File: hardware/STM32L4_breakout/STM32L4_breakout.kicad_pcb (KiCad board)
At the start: 2 copper layers, 84.8 x 91.2 mm, 67 parts, among them J1 12V IN, J10 GPIO, J11 SPI1, J12 USART1, J13 USART3, J14 UART4, J15 3.3V, J16 5V, J17 12V, J2 SWD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

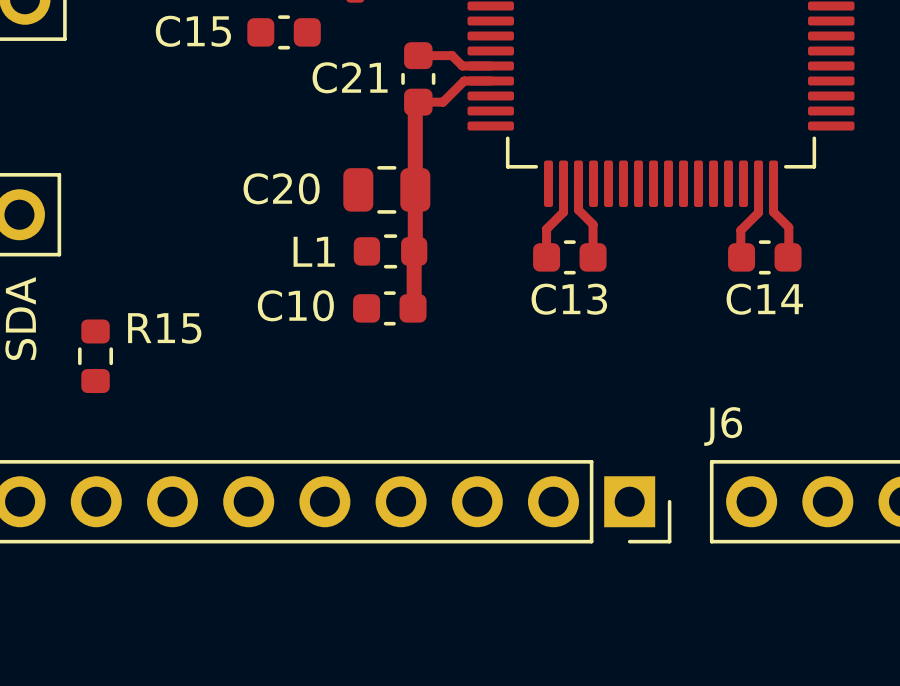
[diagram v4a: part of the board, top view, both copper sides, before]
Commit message: routed SPI lines
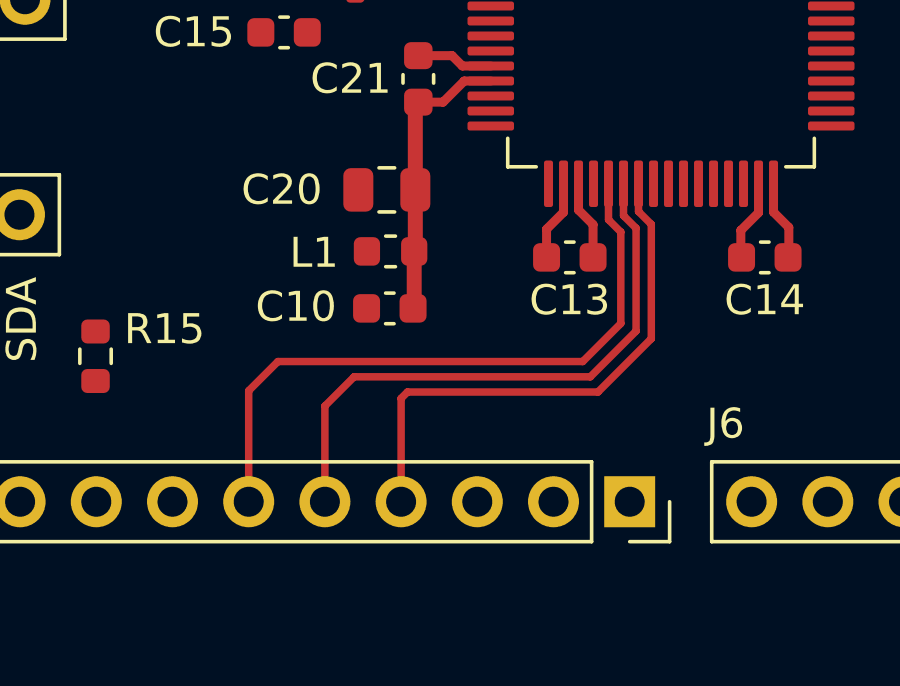
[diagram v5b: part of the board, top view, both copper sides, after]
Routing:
- net SPI1_SCK: track 0.00 -> 21.9 mm
- net SPI1_MISO: track 0.00 -> 19.7 mm
- net SPI1_MOSI: track 0.00 -> 18.0 mm
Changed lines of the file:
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@@
   (segment (start 142.808 65.264) (end 142.788 65.284) (width 0.3) (layer "F.Cu") (net 9))
   (segment (start 142.088 65.764) (end 140.788 65.764) (width 0.3) (layer "F.Cu") (net 9))
+  (segment (start 152.228 73.485208) (end 152.654 73.911208) (width 0.25) (layer "F.Cu") (net 25))
+  (segment (start 150.876 79.502) (end 144.526 79.502) (width 0.25) (layer "F.Cu") (net 25))
+  (segment (start 144.314 79.714) (end 144.314 83.159) (width 0.25) (layer "F.Cu") (net 25))
+  (segment (start 144.526 79.502) (end 144.314 79.714) (width 0.25) (layer "F.Cu") (net 25))
+  (segment (start 152.654 73.911208) (end 152.654 77.724) (width 0.25) (layer "F.Cu") (net 25))
+  (segment (start 152.228 72.559) (end 152.228 73.485208) (width 0.25) (layer "F.Cu") (net 25))
+  (segment (start 152.654 77.724) (end 150.876 79.502) (width 0.25) (layer "F.Cu") (net 25))
+  (segment (start 151.728 73.621604) (end 152.146 74.039604) (width 0.25) (layer "F.Cu") (net 26))
+  (segment (start 142.748 78.994) (end 141.774 79.968) (width 0.25) (layer "F.Cu") (net 26))
+  (segment (start 141.774 79.968) (end 141.774 83.159) (width 0.25) (layer "F.Cu") (net 26))
+  (segment (start 152.146 77.47) (end 150.622 78.994) (width 0.25) (layer "F.Cu") (net 26))
+  (segment (start 152.146 74.039604) (end 152.146 77.47) (width 0.25) (layer "F.Cu") (net 26))
+  (segment (start 150.622 78.994) (end 142.748 78.994) (width 0.25) (layer "F.Cu") (net 26))
+  (segment (start 151.728 72.559) (end 151.728 73.621604) (width 0.25) (layer "F.Cu") (net 26))
+  (segment (start 139.234 83.159) (end 139.234 79.46) (width 0.25) (layer "F.Cu") (net 27))
+  (segment (start 150.368 78.486) (end 151.638 77.216) (width 0.25) (layer "F.Cu") (net 27))
+  (segment (start 139.234 79.46) (end 140.208 78.486) (width 0.25) (layer "F.Cu") (net 27))
+  (segment (start 151.228 73.758) (end 151.228 72.559) (width 0.25) (layer "F.Cu") (net 27))
+  (segment (start 140.208 78.486) (end 150.368 78.486) (width 0.25) (layer "F.Cu") (net 27))
+  (segment (start 151.638 74.168) (end 151.228 73.758) (width 0.25) (layer "F.Cu") (net 27))
+  (segment (start 151.638 77.216) (end 151.638 74.168) (width 0.25) (layer "F.Cu") (net 27))
   (segment (start 146.358 64.134) (end 145.988 63.764) (width 0.3) (layer "F.Cu") (net 56))
   (segment (start 147.303 64.134) (end 146.358 64.134) (width 0.3) (layer "F.Cu") (net 56))

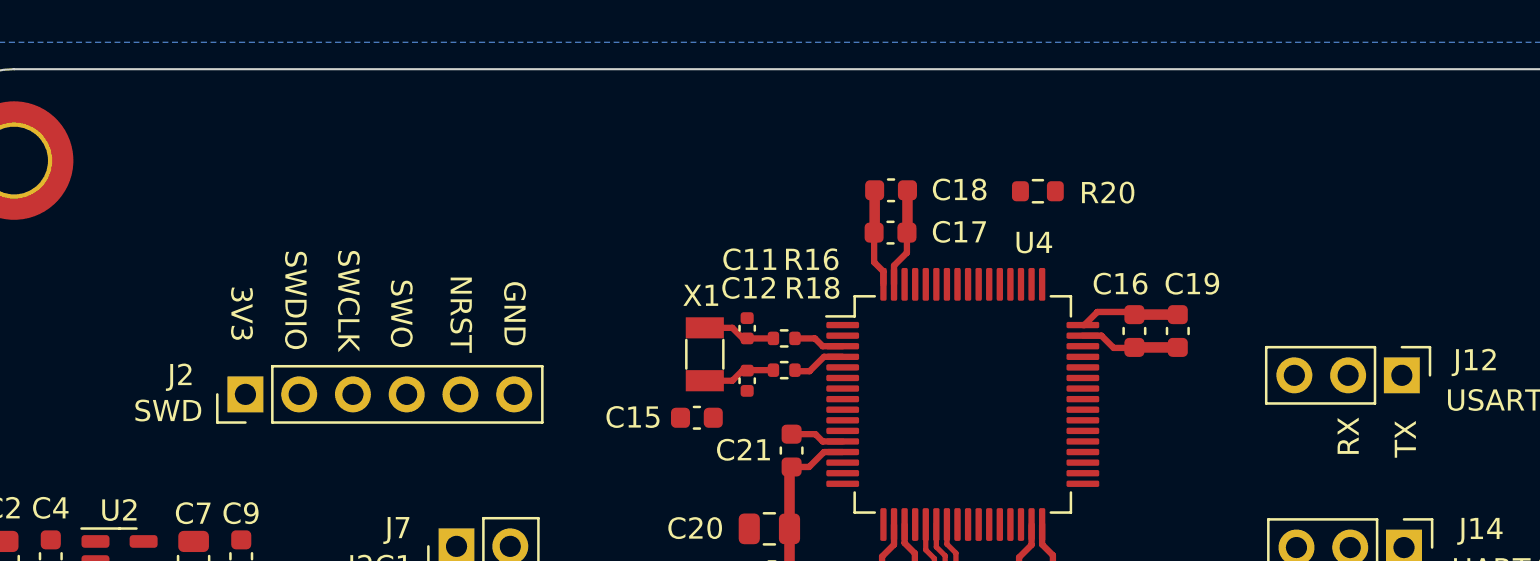
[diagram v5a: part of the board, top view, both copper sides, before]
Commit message: routed SWD on breakout board
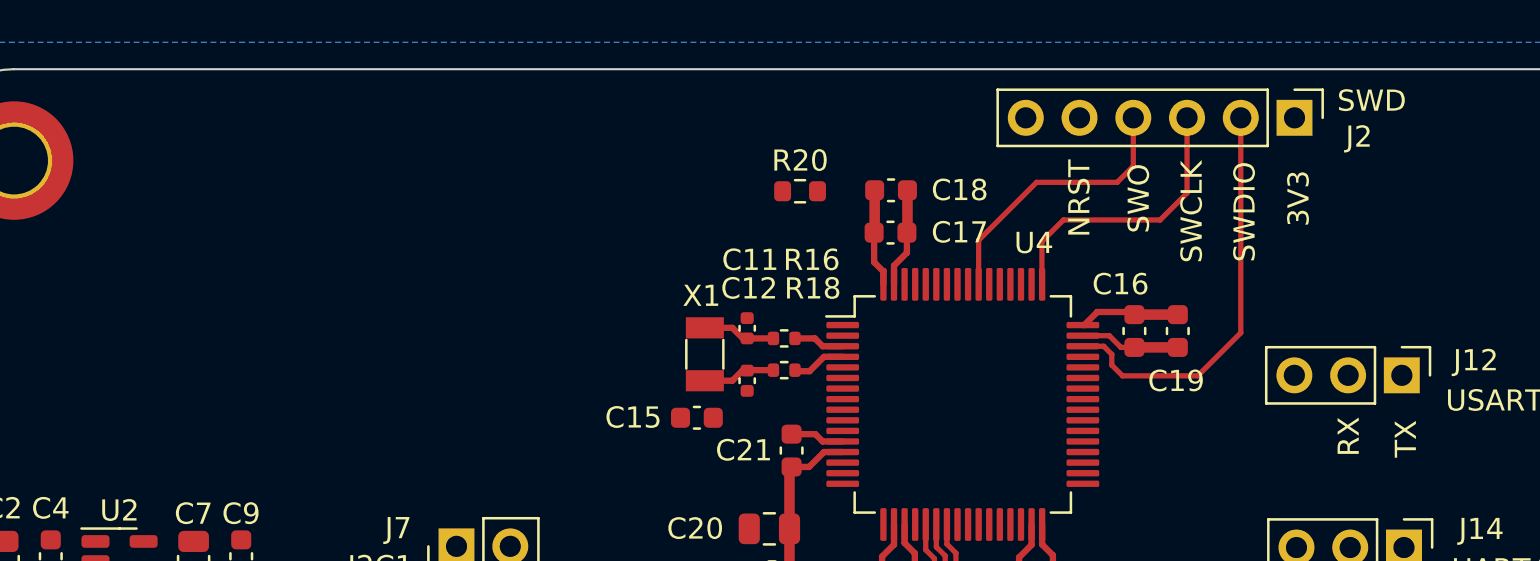
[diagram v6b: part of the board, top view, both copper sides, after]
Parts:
- moved J2 51.3 mm to (168.7, 53.3), turned to -90 degrees
- moved R20 11.2 mm to (145.3, 56.8), turned to 0 degrees
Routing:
- net SWDIO: track 0.00 -> 19.3 mm
- net SWCLK: track 0.00 -> 13.4 mm
- net SWO: track 0.00 -> 13.1 mm
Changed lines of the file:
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@@
   )
   (footprint "Resistor_SMD:R_0603_1608Metric" (layer "F.Cu")
-    (at 156.528 56.809 180)
+    (at 145.288 56.809)
     (descr "Resistor SMD 0603 (1608 Metric), square (rectangular) end terminal, IPC_7351 nominal, (Body size source: IPC-SM-782 page 72, https://www.pcb-3d.com/wordpress/wp-content/uploads/ipc-sm-782a_amendment_1_and_2.pdf), generated with kicad-footprint-generator")
     (tags "resistor")
@@
     (property "Sheetname" "")
     (attr smd)
-    (fp_text reference "R20" (at -3.3 -0.1) (layer "F.SilkS")
+    (fp_text reference "R20" (at 0 -1.437) (layer "F.SilkS")
       (effects (font (size 1 1) (thickness 0.15)))
     )
@@
     (fp_line (start 0.8 0.4125) (end -0.8 0.4125) (layer "F.Fab") (width 0.1))
     (fp_line (start -0.8 0.4125) (end -0.8 -0.4125) (layer "F.Fab") (width 0.1))
-    (pad "1" smd roundrect (at -0.825 0 180) (size 0.8 0.95) (layers "F.Cu" "F.Paste" "F.Mask") (roundrect_rratio 0.25)
+    (pad "1" smd roundrect (at -0.825 0) (size 0.8 0.95) (layers "F.Cu" "F.Paste" "F.Mask") (roundrect_rratio 0.25)
       (net 58 "Net-(R20-Pad1)") (pintype "passive"))
-    (pad "2" smd roundrect (at 0.825 0 180) (size 0.8 0.95) (layers "F.Cu" "F.Paste" "F.Mask") (roundrect_rratio 0.25)
+    (pad "2" smd roundrect (at 0.825 0) (size 0.8 0.95) (layers "F.Cu" "F.Paste" "F.Mask") (roundrect_rratio 0.25)
       (net 59 "/BOOT0") (pintype "passive"))
     (model "${KICAD6_3DMODEL_DIR}/Resistor_SMD.3dshapes/R_0603_1608Metric.wrl"
@@
   )
   (footprint "Connector_PinHeader_2.54mm:PinHeader_1x06_P2.54mm_Vertical" (layer "F.Cu")
-    (at 119.078 66.409 90)
+    (at 168.656 53.34 -90)
     (descr "Through hole straight pin header, 1x06, 2.54mm pitch, single row")
     (tags "Through hole pin header THT 1x06 2.54mm single row")
@@
     (property "Sheetname" "")
     (attr through_hole)
-    (fp_text reference "J2" (at 0.9 -3.05 180) (layer "F.SilkS")
-      (effects (font (size 1 1) (thickness 0.15)))
-    )
-    (fp_text value "SWD" (at -0.8 -3.65 180) (layer "F.SilkS")
-      (effects (font (size 1 1) (thickness 0.15)))
-    )
-    (fp_text user "SWO" (at 3.81 7.35 -90 unlocked) (layer "F.SilkS")
-      (effects (font (size 1 1) (thickness 0.15)))
-    )
-    (fp_text user "NRST" (at 3.81 10.16 -90 unlocked) (layer "F.SilkS")
-      (effects (font (size 1 1) (thickness 0.15)))
-    )
-    (fp_text user "SWDIO" (at 4.445 2.35 -90 unlocked) (layer "F.SilkS")
-      (effects (font (size 1 1) (thickness 0.15)))
-    )
-    (fp_text user "SWCLK" (at 4.445 4.85 -90 unlocked) (layer "F.SilkS")
-      (effects (font (size 1 1) (thickness 0.15)))
-    )
-    (fp_text user "3V3" (at 3.81 -0.2 -90 unlocked) (layer "F.SilkS")
-      (effects (font (size 1 1) (thickness 0.15)))
-    )
-    (fp_text user "GND" (at 3.81 12.7 -90 unlocked) (layer "F.SilkS")
+    (fp_text reference "J2" (at 0.9 -3.05) (layer "F.SilkS")
+      (effects (font (size 1 1) (thickness 0.15)))
+    )
+    (fp_text value "SWD" (at -0.8 -3.65) (layer "F.SilkS")
+      (effects (font (size 1 1) (thickness 0.15)))
+    )
+    (fp_text user "SWO" (at 3.81 7.35 -270 unlocked) (layer "F.SilkS")
+      (effects (font (size 1 1) (thickness 0.15)))
+    )
+    (fp_text user "NRST" (at 3.81 10.16 -270 unlocked) (layer "F.SilkS")
+      (effects (font (size 1 1) (thickness 0.15)))
+    )
+    (fp_text user "SWDIO" (at 4.445 2.35 -270 unlocked) (layer "F.SilkS")
+      (effects (font (size 1 1) (thickness 0.15)))
+    )
+    (fp_text user "SWCLK" (at 4.445 4.85 -270 unlocked) (layer "F.SilkS")
+      (effects (font (size 1 1) (thickness 0.15)))
+    )
+    (fp_text user "3V3" (at 3.81 -0.2 -270 unlocked) (layer "F.SilkS")
       (effects (font (size 1 1) (thickness 0.15)))
     )
@@
     (fp_line (start 1.27 13.97) (end -1.27 13.97) (layer "F.Fab") (width 0.1))
     (fp_line (start 1.27 -1.27) (end 1.27 13.97) (layer "F.Fab") (width 0.1))
-    (pad "1" thru_hole rect (at 0 0 90) (size 1.7 1.7) (drill 1) (layers *.Cu *.Mask)
+    (pad "1" thru_hole rect (at 0 0 270) (size 1.7 1.7) (drill 1) (layers *.Cu *.Mask)
       (net 5 "VMEM") (pinfunction "Pin_1") (pintype "passive"))
-    (pad "2" thru_hole oval (at 0 2.54 90) (size 1.7 1.7) (drill 1) (layers *.Cu *.Mask)
+    (pad "2" thru_hole oval (at 0 2.54 270) (size 1.7 1.7) (drill 1) (layers *.Cu *.Mask)
       (net 11 "SWDIO") (pinfunction "Pin_2") (pintype "passive"))
-    (pad "3" thru_hole oval (at 0 5.08 90) (size 1.7 1.7) (drill 1) (layers *.Cu *.Mask)
+    (pad "3" thru_hole oval (at 0 5.08 270) (size 1.7 1.7) (drill 1) (layers *.Cu *.Mask)
       (net 12 "SWCLK") (pinfunction "Pin_3") (pintype "passive"))
-    (pad "4" thru_hole oval (at 0 7.62 90) (size 1.7 1.7) (drill 1) (layers *.Cu *.Mask)
+    (pad "4" thru_hole oval (at 0 7.62 270) (size 1.7 1.7) (drill 1) (layers *.Cu *.Mask)
       (net 13 "SWO") (pinfunction "Pin_4") (pintype "passive"))
-    (pad "5" thru_hole oval (at 0 10.16 90) (size 1.7 1.7) (drill 1) (layers *.Cu *.Mask)
+    (pad "5" thru_hole oval (at 0 10.16 270) (size 1.7 1.7) (drill 1) (layers *.Cu *.Mask)
       (net 10 "STM_NRST") (pinfunction "Pin_5") (pintype "passive"))
-    (pad "6" thru_hole oval (at 0 12.7 90) (size 1.7 1.7) (drill 1) (layers *.Cu *.Mask)
+    (pad "6" thru_hole oval (at 0 12.7 270) (size 1.7 1.7) (drill 1) (layers *.Cu *.Mask)
       (net 2 "GND") (pinfunction "Pin_6") (pintype "passive"))
     (model "${KICAD6_3DMODEL_DIR}/Connector_PinHeader_2.54mm.3dshapes/PinHeader_1x06_P2.54mm_Vertical.wrl"
@@
     (property "Sheetname" "")
     (attr smd)
-    (fp_text reference "C19" (at -2.2 -0.7) (layer "F.SilkS")
+    (fp_text reference "C19" (at 2.372 0.07) (layer "F.SilkS")
       (effects (font (size 1 1) (thickness 0.15)))
     )
@@
   (segment (start 155.638 74.114) (end 155.638 74.989) (width 0.3) (layer "F.Cu") (net 2))
   (segment (start 149.238 74.939) (end 149.163 75.014) (width 0.3) (layer "F.Cu") (net 2))
+  (segment (start 158.653 63.634) (end 159.9 63.634) (width 0.25) (layer "F.Cu") (net 2))
+  (segment (start 159.9 63.634) (end 160.455 64.189) (width 0.25) (layer "F.Cu") (net 2))
   (segment (start 163.138 64.189) (end 161.088 64.189) (width 0.5) (layer "F.Cu") (net 2))
-  (segment (start 159.529041 63.634) (end 160.109041 64.214) (width 0.3) (layer "F.Cu") (net 2))
   (segment (start 150.338 59.714) (end 150.338 58.764) (width 0.3) (layer "F.Cu") (net 2))
   (segment (start 149.728 61.209) (end 149.728 60.324) (width 0.3) (layer "F.Cu") (net 2))
@@
   (segment (start 156.228 73.524) (end 155.638 74.114) (width 0.3) (layer "F.Cu") (net 2))
   (segment (start 150.363 56.764) (end 150.363 58.739) (width 0.5) (layer "F.Cu") (net 2))
-  (segment (start 160.109041 64.214) (end 161.063 64.214) (width 0.3) (layer "F.Cu") (net 2))
   (segment (start 161.063 64.214) (end 161.088 64.189) (width 0.3) (layer "F.Cu") (net 2))
-  (segment (start 158.653 63.634) (end 159.529041 63.634) (width 0.3) (layer "F.Cu") (net 2))
+  (segment (start 160.455 64.189) (end 161.088 64.189) (width 0.25) (layer "F.Cu") (net 2))
   (segment (start 146.013 68.289) (end 144.888 68.289) (width 0.3) (layer "F.Cu") (net 2))
   (segment (start 146.358 68.634) (end 146.013 68.289) (width 0.3) (layer "F.Cu") (net 2))
@@
   (segment (start 142.808 65.264) (end 142.788 65.284) (width 0.3) (layer "F.Cu") (net 9))
   (segment (start 142.088 65.764) (end 140.788 65.764) (width 0.3) (layer "F.Cu") (net 9))
+  (segment (start 164.084 65.532) (end 166.116 63.5) (width 0.25) (layer "F.Cu") (net 11))
+  (segment (start 158.653 64.134) (end 159.638 64.134) (width 0.25) (layer "F.Cu") (net 11))
+  (segment (start 160.02 64.516) (end 160.02 65.024) (width 0.25) (layer "F.Cu") (net 11))
+  (segment (start 160.528 65.532) (end 164.084 65.532) (width 0.25) (layer "F.Cu") (net 11))
+  (segment (start 160.02 65.024) (end 160.528 65.532) (width 0.25) (layer "F.Cu") (net 11))
+  (segment (start 166.116 63.5) (end 166.116 53.34) (width 0.25) (layer "F.Cu") (net 11))
+  (segment (start 159.638 64.134) (end 160.02 64.516) (width 0.25) (layer "F.Cu") (net 11))
+  (segment (start 156.728 61.209) (end 156.718 61.199) (width 0.25) (layer "F.Cu") (net 12))
+  (segment (start 157.734 58.166) (end 162.306 58.166) (width 0.25) (layer "F.Cu") (net 12))
+  (segment (start 163.576 56.896) (end 163.576 53.34) (width 0.25) (layer "F.Cu") (net 12))
+  (segment (start 156.718 61.199) (end 156.718 59.182) (width 0.25) (layer "F.Cu") (net 12))
+  (segment (start 156.718 59.182) (end 157.734 58.166) (width 0.25) (layer "F.Cu") (net 12))
+  (segment (start 162.306 58.166) (end 163.576 56.896) (width 0.25) (layer "F.Cu") (net 12))
+  (segment (start 161.036 55.626) (end 161.036 53.34) (width 0.25) (layer "F.Cu") (net 13))
+  (segment (start 153.728 61.209) (end 153.728 59.124) (width 0.25) (layer "F.Cu") (net 13))
+  (segment (start 156.464 56.388) (end 160.274 56.388) (width 0.25) (layer "F.Cu") (net 13))
+  (segment (start 153.728 59.124) (end 156.464 56.388) (width 0.25) (layer "F.Cu") (net 13))
+  (segment (start 160.274 56.388) (end 161.036 55.626) (width 0.25) (layer "F.Cu") (net 13))
   (segment (start 152.228 73.485208) (end 152.654 73.911208) (width 0.25) (layer "F.Cu") (net 25))
   (segment (start 150.876 79.502) (end 144.526 79.502) (width 0.25) (layer "F.Cu") (net 25))
@@
       2cbdb457-9987-4ddc-93e8-d4dd9d286470
       2d5bffe8-9ded-4b64-bd38-1e92a2f27edb
-      2d7dcd00-b860-48f2-92f2-a9abaed5d498
       30a5ac2b-899f-4f4a-8982-17bbb1f18aa3
       30df35bf-2f83-4d2c-8cbe-2322b71f1c28
@@
       9af6c6cf-1f9d-4130-80bb-99b34729bd0c
       9ca6006b-e6fe-47ac-be55-5d74af5a935d
-      9cfdef60-6d45-408c-96fd-3ce10f48aab0
       9d4ca5fa-7b48-4632-b5f3-0f5dc28f0e8c
       9f6084b2-22b1-4697-a915-1f4522a1da56
@@
       a0f7c665-b523-4a45-85b2-86bf1ea802ba
       a295ce74-c53c-4019-9e30-11f67a541312
-      a3c82da3-e83e-45b3-a721-77c95fd23f10
       a8fb4bd1-792a-432d-999d-676f1bd093dd
       aaf7c52f-dc4c-4d02-b939-3e12f1355ad3

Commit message: breakout board signal routing WIP
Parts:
- moved J9 60.0 mm to (121.4, 69.3), turned to 90 degrees
- moved C2 53.8 mm to (156.6, 96.6)
- moved C4 53.8 mm to (158.9, 96.3)
- moved C6 53.8 mm to (164.1, 99.3)
- moved C7 53.8 mm to (165.6, 96.6)
- moved C9 53.8 mm to (167.9, 96.3)
- moved U2 53.8 mm to (162.1, 96.6)
- moved J14 50.0 mm to (124.0, 77.0)
- moved J12 49.8 mm to (124.0, 63.2)
- moved J11 41.6 mm to (174.0, 70.1)
- moved J8 38.6 mm to (183.6, 86.4), turned to 180 degrees
- moved J13 26.6 mm to (183.4, 70.1)
- moved J7 19.1 mm to (121.4, 56.1)
- moved R2 16.8 mm to (168.3, 118.4)
- moved R6 16.8 mm to (168.4, 112.9)
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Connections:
- J12 pad 1: USART1_RX -> USART1_TX
- J12 pad 2: USART1_TX -> USART1_RX
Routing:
- net I2C1_SCL: track 0.00 -> 38.8 mm
- net I2C1_SDA: track 0.00 -> 34.5 mm
- net STM_NRST: track 0.00 -> 18.9 mm, vias 0 -> 2
- net +3.3V: track 14.8 -> 15.7 mm
- net GND: track 17.5 -> 18.0 mm
